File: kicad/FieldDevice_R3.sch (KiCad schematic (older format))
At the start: 0 parts

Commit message: Progressive checkin
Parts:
- added C?: C, symbol Device:C
- added C?: 100nF, symbol Device:C
- added C? (x2): 1 µF 16V, symbol Device:C
- added H?: DIGI_XBEE-XBee-Adapter, symbol FieldDevice_R3_Symbols:DIGI_XBEE-XBee-Adapter
- added J?: V in 6-18V, Pin_Headers:Pin_Header_Angled_1x02_Pitch2.54mm, symbol FieldDevice_Power_5V-rescue:Conn_01x02_Male-FieldDevice_Power_5V-rescue
- added J?: Vin+, symbol Connector:Conn_01x01_Female
- added J?: Vin-, symbol Connector:Conn_01x01_Female
- added JP? (x2): SolderJumper_2_Open, symbol Jumper:SolderJumper_2_Open
- added U?: INA219AxD, Package_SO:SOIC-8_3.9x4.9mm_P1.27mm, symbol Analog_ADC:INA219AxD
- added U?: EA_DOGS104x-A, symbol FieldDevice_R3_Symbols:EA_DOGS104x-A
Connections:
- net labels added: 3V3_Vcc, 5_Vss, GND, SCL, SDA
- wire segments 0 -> 53
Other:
- note added: "A1 A2 Address\n——————————————\nGND GND 1000000\nGND VS+ 1000001\nGND SDA 1000010\nGND SCL 1000011\nVS+ GND 1000100\nVS+ VS+ 1000101\nVS+ SDA 1000110\nVS+ SCL 1000111\nSDA GND 1001000\nSDA VS+ 1001001\nSDA SDA 1001010\nSDA SCL 1001011\nSCL GND 1001100\nSCL VS+ 1001101\nSCL SDA 1001110\nSCL SCL 1001111"
- note added: "ATTiny1607 \nDS7505\n"
- note added: "Display"
- note added: "Sensor"
- note added: "TPS54232"
- note added: "Telemetry"

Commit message: Updates and new features
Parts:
- added JP103: 0x7A, symbol Jumper:SolderJumper_2_Open
- added JP104: 0x78, symbol Jumper:SolderJumper_2_Open
- added R101: 1 mΩ 1% 1W, Resistor_SMD:R_2010_5025Metric, symbol Device:R
- C101: renamed from C?; value C -> 100nF; footprint (none) -> Capacitor_SMD:C_0805_2012Metric
- C102, C103, C104: renamed from C?; footprint (none) -> Capacitor_SMD:C_0805_2012Metric
- gave numbers to parts that had none: 8
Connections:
- net labels added: IIC, ~RESET
- wire segments 53 -> 89
- no-connect marks 0 -> 4
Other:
- note added: "SA0=GND: ADDR 0x78\nSDA=Vdd: ADR=0x7A"
- moved on the sheet: C103, C104, J101, J102, U102

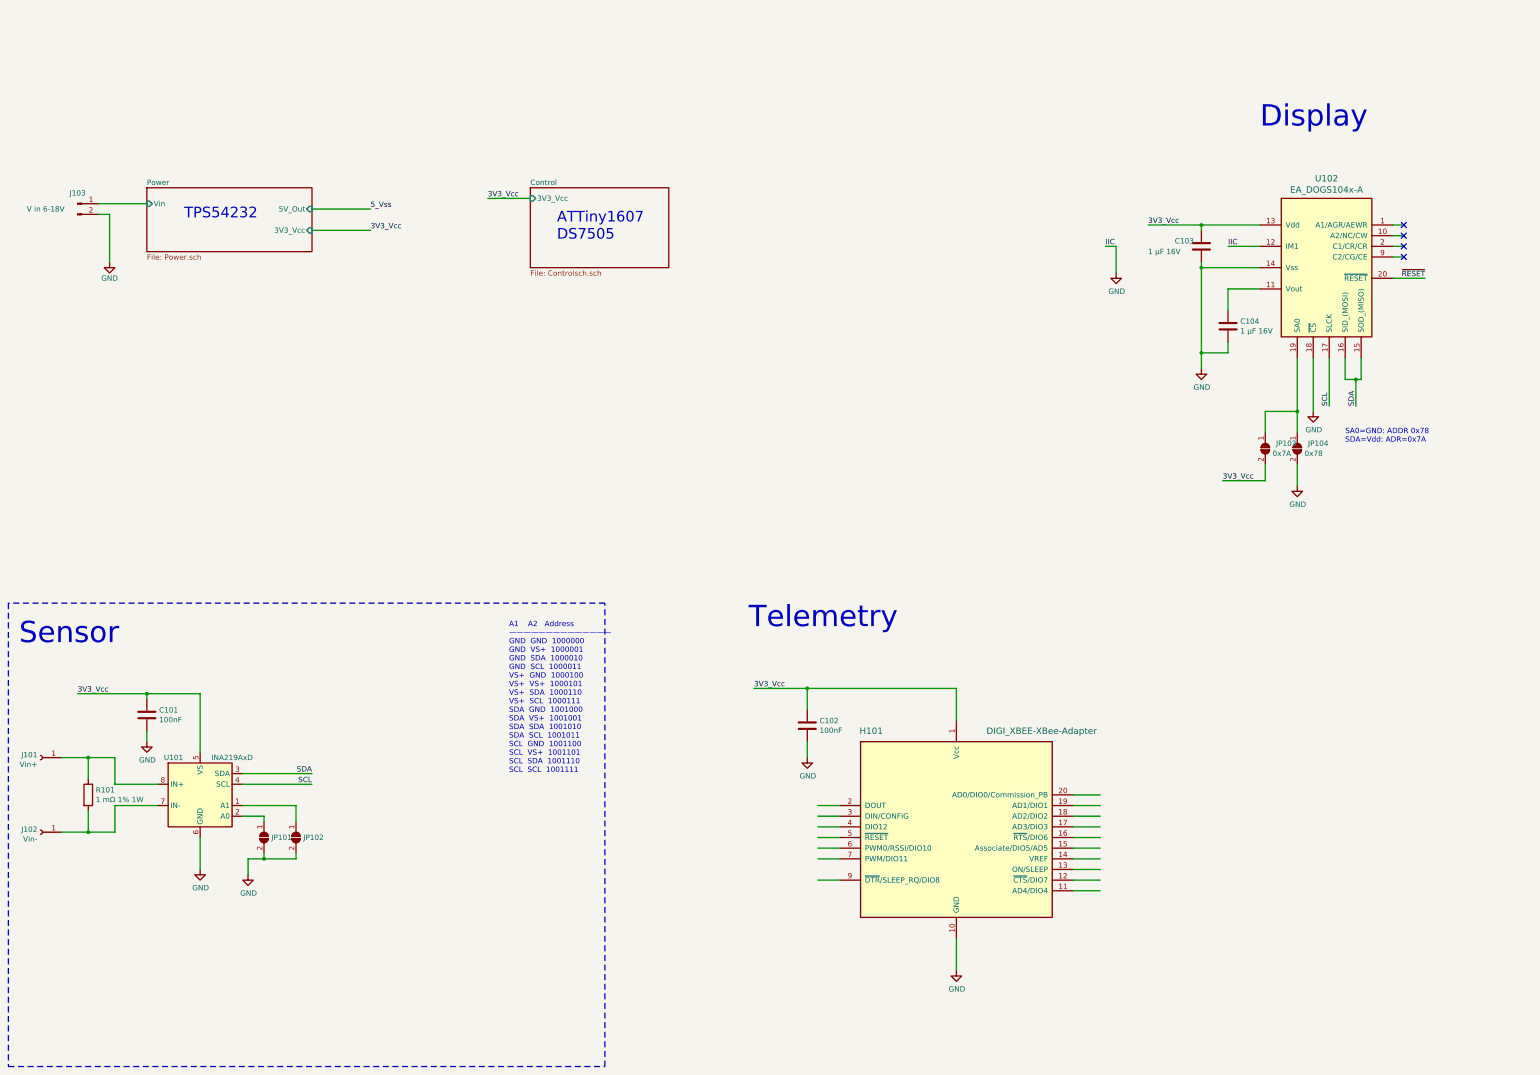
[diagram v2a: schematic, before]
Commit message: Updated the addresssing of the LCD
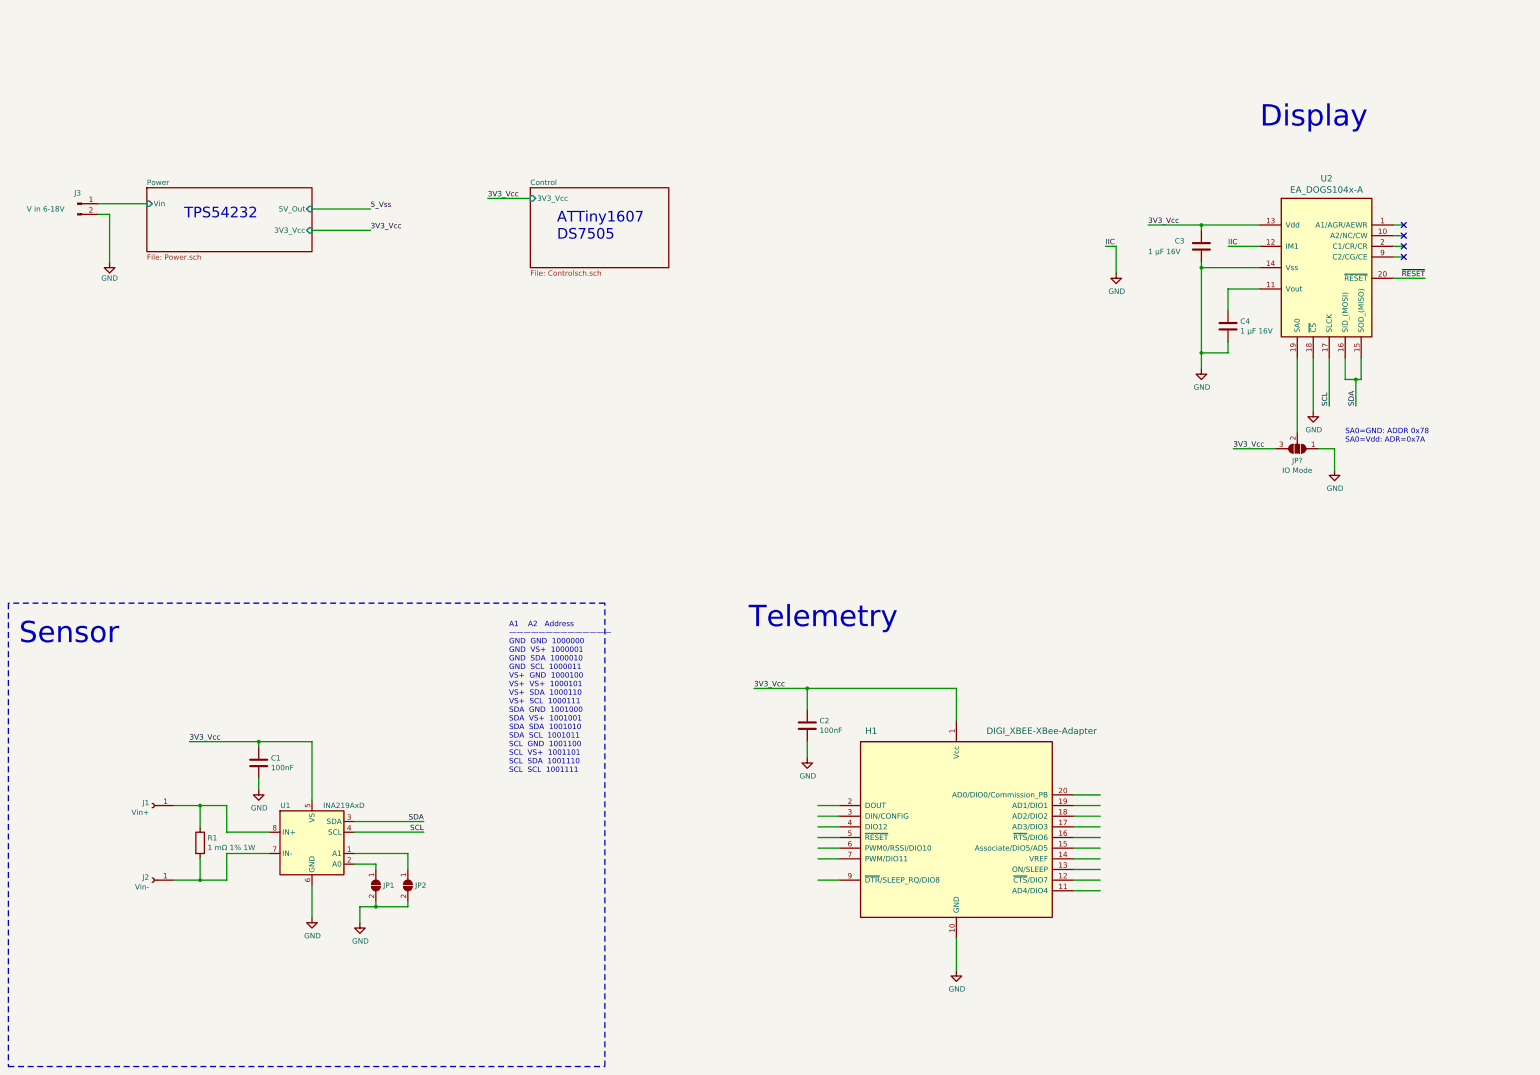
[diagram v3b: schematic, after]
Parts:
- removed JP103: 0x7A, symbol Jumper:SolderJumper_2_Open
- removed JP104: 0x78, symbol Jumper:SolderJumper_2_Open
- added JP?: IO Mode, symbol Jumper:SolderJumper_3_Open
- renumbered C101 to C1, C102 to C2, C103 to C3, C104 to C4, H101 to H1, J101 to J1, J102 to J2, J103 to J3, JP101 to JP1, JP102 to JP2, R101 to R1, U101 to U1, U102 to U2
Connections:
- wire segments 89 -> 86
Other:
- note added: "SA0=GND: ADDR 0x78\nSA0=Vdd: ADR=0x7A"
- note removed: "SA0=GND: ADDR 0x78\nSDA=Vdd: ADR=0x7A"
- moved on the sheet: C1, J1, J2, JP1, JP2, R1, U1

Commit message: Updates the RC selection for the switch debounce
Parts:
- JP103: renamed from JP?; value IO Mode -> IIC ADDR
- renumbered C1 to C101, C2 to C102, C3 to C103, C4 to C104, H1 to H101, J3 to J101, J1 to J102, J2 to J103, JP1 to JP101, JP2 to JP102, R1 to R101, U1 to U101, U2 to U102
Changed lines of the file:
@@
 P 1450 2600
 AR Path="/5F21BAEC/5F273CF5" Ref="J?"  Part="1"
-AR Path="/5F273CF5" Ref="J3"  Part="1"
-F 0 "J3" H 1450 2700 50  0000 C CNN
+AR Path="/5F273CF5" Ref="J101"  Part="1"
+F 0 "J101" H 1450 2700 50  0000 C CNN
 F 1 "V in 6-18V" H 1150 2550 50  0000 C CNN
 F 2 "Pin_Headers:Pin_Header_Angled_1x02_Pitch2.54mm" H 1450 2600 50  0001 C CNN
@@
 P 1750 3150
 AR Path="/5F21BAEC/5F273CFB" Ref="#PWR?"  Part="1"
-AR Path="/5F273CFB" Ref="#PWR01"  Part="1"
-F 0 "#PWR01" H 1750 2900 50  0001 C CNN
+AR Path="/5F273CFB" Ref="#PWR0101"  Part="1"
+F 0 "#PWR0101" H 1750 2900 50  0001 C CNN
 F 1 "GND" H 1750 3000 50  0000 C CNN
 F 2 "" H 1750 3150 50  0001 C CNN
@@
 P 3650 8600
 AR Path="/5F21BB38/5F2D6DC8" Ref="U?"  Part="1"
-AR Path="/5F2D6DC8" Ref="U1"  Part="1"
-F 0 "U1" H 3400 8950 50  0000 C CNN
+AR Path="/5F2D6DC8" Ref="U101"  Part="1"
+F 0 "U101" H 3400 8950 50  0000 C CNN
 F 1 "INA219AxD" H 3950 8950 50  0000 C CNN
 F 2 "Package_SO:SOIC-8_3.9x4.9mm_P1.27mm" H 4450 8250 50  0001 C CNN
@@
 P 3650 9300
 AR Path="/5F21BB38/5F2D6DCF" Ref="#PWR?"  Part="1"
-AR Path="/5F2D6DCF" Ref="#PWR03"  Part="1"
-F 0 "#PWR03" H 3650 9050 50  0001 C CNN
+AR Path="/5F2D6DCF" Ref="#PWR0103"  Part="1"
+F 0 "#PWR0103" H 3650 9050 50  0001 C CNN
 F 1 "GND" H 3655 9127 50  0000 C CNN
 F 2 "" H 3650 9300 50  0001 C CNN
@@
 P 3150 7850
 AR Path="/5F21BB38/5F2D6DD8" Ref="C?"  Part="1"
-AR Path="/5F2D6DD8" Ref="C1"  Part="1"
-F 0 "C1" H 3265 7896 50  0000 L CNN
+AR Path="/5F2D6DD8" Ref="C101"  Part="1"
+F 0 "C101" H 3265 7896 50  0000 L CNN
 F 1 "100nF" H 3265 7805 50  0000 L CNN
 F 2 "Capacitor_SMD:C_0805_2012Metric" H 3188 7700 50  0001 C CNN
@@
 P 3150 8100
 AR Path="/5F21BB38/5F2D6DE2" Ref="#PWR?"  Part="1"
-AR Path="/5F2D6DE2" Ref="#PWR02"  Part="1"
-F 0 "#PWR02" H 3150 7850 50  0001 C CNN
+AR Path="/5F2D6DE2" Ref="#PWR0102"  Part="1"
+F 0 "#PWR0102" H 3150 7850 50  0001 C CNN
 F 1 "GND" H 3155 7927 50  0000 C CNN
 F 2 "" H 3150 8100 50  0001 C CNN
@@
 P 4250 9000
 AR Path="/5F21BB38/5F2D6DEC" Ref="JP?"  Part="1"
-AR Path="/5F2D6DEC" Ref="JP1"  Part="1"
-F 0 "JP1" V 4250 9068 50  0000 L CNN
+AR Path="/5F2D6DEC" Ref="JP101"  Part="1"
+F 0 "JP101" V 4250 9068 50  0000 L CNN
 F 1 "SolderJumper_2_Open" V 4295 9068 50  0001 L CNN
 F 2 "" H 4250 9000 50  0001 C CNN
@@
 P 4550 9000
 AR Path="/5F21BB38/5F2D6DF2" Ref="JP?"  Part="1"
-AR Path="/5F2D6DF2" Ref="JP2"  Part="1"
-F 0 "JP2" V 4550 9068 50  0000 L CNN
+AR Path="/5F2D6DF2" Ref="JP102"  Part="1"
+F 0 "JP102" V 4550 9068 50  0000 L CNN
 F 1 "SolderJumper_2_Open" V 4595 9068 50  0001 L CNN
 F 2 "" H 4550 9000 50  0001 C CNN
@@
 P 4100 9350
 AR Path="/5F21BB38/5F2D6DF8" Ref="#PWR?"  Part="1"
-AR Path="/5F2D6DF8" Ref="#PWR04"  Part="1"
-F 0 "#PWR04" H 4100 9100 50  0001 C CNN
+AR Path="/5F2D6DF8" Ref="#PWR0104"  Part="1"
+F 0 "#PWR0104" H 4100 9100 50  0001 C CNN
 F 1 "GND" H 4105 9177 50  0000 C CNN
 F 2 "" H 4100 9350 50  0001 C CNN
@@
 3V3_Vcc
 $Comp
-L Connector:Conn_01x01_Female J2
+L Connector:Conn_01x01_Female J103
 U 1 1 5F27CA6F
 P 2150 8950
-F 0 "J2" H 2178 8976 50  0000 L CNN
+F 0 "J103" H 2178 8976 50  0000 L CNN
 F 1 "Vin-" H 2178 8885 50  0000 L CNN
 F 2 "" H 2150 8950 50  0001 C CNN
@@
 $EndComp
 $Comp
-L Connector:Conn_01x01_Female J1
+L Connector:Conn_01x01_Female J102
 U 1 1 5F27B9E4
 P 2150 8250
-F 0 "J1" H 2178 8276 50  0000 L CNN
+F 0 "J102" H 2178 8276 50  0000 L CNN
 F 1 "Vin+" H 2178 8185 50  0000 L CNN
 F 2 "" H 2150 8250 50  0001 C CNN
@@
 P 9700 8500
 AR Path="/5F21BBDC/5F2E9CD0" Ref="H?"  Part="1"
-AR Path="/5F2E9CD0" Ref="H1"  Part="1"
-F 0 "H1" H 8900 9450 60  0000 C CNN
+AR Path="/5F2E9CD0" Ref="H101"  Part="1"
+F 0 "H101" H 8900 9450 60  0000 C CNN
 F 1 "DIGI_XBEE-XBee-Adapter" H 10500 9450 60  0000 C CNN
 F 2 "" H 9050 8300 60  0000 C CNN
@@
 P 9700 9800
 AR Path="/5F21BBDC/5F2E9CDA" Ref="#PWR?"  Part="1"
-AR Path="/5F2E9CDA" Ref="#PWR06"  Part="1"
-F 0 "#PWR06" H 9700 9550 50  0001 C CNN
+AR Path="/5F2E9CDA" Ref="#PWR0106"  Part="1"
+F 0 "#PWR0106" H 9700 9550 50  0001 C CNN
 F 1 "GND" H 9705 9627 50  0000 C CNN
 F 2 "" H 9700 9800 50  0001 C CNN
@@
 P 8300 7500
 AR Path="/5F21BBDC/5F2E9CE0" Ref="C?"  Part="1"
-AR Path="/5F2E9CE0" Ref="C2"  Part="1"
-F 0 "C2" H 8415 7546 50  0000 L CNN
+AR Path="/5F2E9CE0" Ref="C102"  Part="1"
+F 0 "C102" H 8415 7546 50  0000 L CNN
 F 1 "100nF" H 8415 7455 50  0000 L CNN
 F 2 "Capacitor_SMD:C_0805_2012Metric" H 8338 7350 50  0001 C CNN
@@
 P 8300 7800
 AR Path="/5F21BBDC/5F2E9CEA" Ref="#PWR?"  Part="1"
-AR Path="/5F2E9CEA" Ref="#PWR05"  Part="1"
-F 0 "#PWR05" H 8300 7550 50  0001 C CNN
+AR Path="/5F2E9CEA" Ref="#PWR0105"  Part="1"
+F 0 "#PWR0105" H 8300 7550 50  0001 C CNN
 F 1 "GND" H 8305 7627 50  0000 C CNN
 F 2 "" H 8300 7800 50  0001 C CNN
@@
 Telemetry
 $Comp
-L FieldDevice_R3_Symbols:EA_DOGS104x-A U2
+L FieldDevice_R3_Symbols:EA_DOGS104x-A U102
 U 1 1 5F2F0B8A
 P 13200 3200
-F 0 "U2" H 13175 4037 60  0000 C CNN
+F 0 "U102" H 13175 4037 60  0000 C CNN
 F 1 "EA_DOGS104x-A" H 13175 3931 60  0000 C CNN
 F 2 "" H 13250 3200 60  0001 C CNN
@@
 P 12000 3000
 AR Path="/5F21BBDC/5F300DA6" Ref="C?"  Part="1"
-AR Path="/5F300DA6" Ref="C3"  Part="1"
-F 0 "C3" H 11750 3050 50  0000 L CNN
+AR Path="/5F300DA6" Ref="C103"  Part="1"
+F 0 "C103" H 11750 3050 50  0000 L CNN
 F 1 "1 µF 16V" H 11500 2950 50  0000 L CNN
 F 2 "Capacitor_SMD:C_0805_2012Metric" H 12038 2850 50  0001 C CNN
@@
 P 12250 3750
 AR Path="/5F21BBDC/5F305F02" Ref="C?"  Part="1"
-AR Path="/5F305F02" Ref="C4"  Part="1"
-F 0 "C4" H 12365 3796 50  0000 L CNN
+AR Path="/5F305F02" Ref="C104"  Part="1"
+F 0 "C104" H 12365 3796 50  0000 L CNN
 F 1 "1 µF 16V" H 12365 3705 50  0000 L CNN
 F 2 "Capacitor_SMD:C_0805_2012Metric" H 12288 3600 50  0001 C CNN
@@
 P 12000 4150
 AR Path="/5F21BBDC/5F3097E1" Ref="#PWR?"  Part="1"
-AR Path="/5F3097E1" Ref="#PWR08"  Part="1"
-F 0 "#PWR08" H 12000 3900 50  0001 C CNN
+AR Path="/5F3097E1" Ref="#PWR0108"  Part="1"
+F 0 "#PWR0108" H 12000 3900 50  0001 C CNN
 F 1 "GND" H 12005 3977 50  0000 C CNN
 F 2 "" H 12000 4150 50  0001 C CNN
@@
 	13800 2800 13900 2800
 $Comp
-L Device:R R1
+L Device:R R101
 U 1 1 5F833947
 P 2600 8600
-F 0 "R1" H 2670 8646 50  0000 L CNN
+F 0 "R101" H 2670 8646 50  0000 L CNN
 F 1 "1 mΩ 1% 1W" H 2670 8555 50  0000 L CNN
 F 2 "Resistor_SMD:R_2010_5025Metric" V 2530 8600 50  0001 C CNN
@@
 P 13050 4550
 AR Path="/5F21BBDC/5F8701C1" Ref="#PWR?"  Part="1"
-AR Path="/5F8701C1" Ref="#PWR010"  Part="1"
-F 0 "#PWR010" H 13050 4300 50  0001 C CNN
+AR Path="/5F8701C1" Ref="#PWR0109"  Part="1"
+F 0 "#PWR0109" H 13050 4300 50  0001 C CNN
 F 1 "GND" H 13055 4377 50  0000 C CNN
 F 2 "" H 13050 4550 50  0001 C CNN
@@
 P 13250 5100
 AR Path="/5F21BBDC/5F88699F" Ref="#PWR?"  Part="1"
-AR Path="/5F88699F" Ref="#PWR09"  Part="1"
-F 0 "#PWR09" H 13250 4850 50  0001 C CNN
+AR Path="/5F88699F" Ref="#PWR0110"  Part="1"
+F 0 "#PWR0110" H 13250 4850 50  0001 C CNN
 F 1 "GND" H 13255 4927 50  0000 C CNN
 F 2 "" H 13250 5100 50  0001 C CNN
@@
 P 11200 3250
 AR Path="/5F21BBDC/5F8E52C9" Ref="#PWR?"  Part="1"
-AR Path="/5F8E52C9" Ref="#PWR07"  Part="1"
-F 0 "#PWR07" H 11200 3000 50  0001 C CNN
+AR Path="/5F8E52C9" Ref="#PWR0107"  Part="1"
+F 0 "#PWR0107" H 11200 3000 50  0001 C CNN
 F 1 "GND" H 11205 3077 50  0000 C CNN
 F 2 "" H 11200 3250 50  0001 C CNN
@@
 	11200 3000 11100 3000
 $Comp
-L Jumper:SolderJumper_3_Open JP?
+L Jumper:SolderJumper_3_Open JP103
 U 1 1 5F907468
 P 12900 4900
-F 0 "JP?" H 12900 5013 50  0000 C CNN
-F 1 "IO Mode" H 12900 5104 50  0000 C CNN
+F 0 "JP103" H 12900 5013 50  0000 C CNN
+F 1 "IIC ADDR" H 12900 5104 50  0000 C CNN
 F 2 "" H 12900 4900 50  0001 C CNN
 F 3 "~" H 12900 4900 50  0001 C CNN
